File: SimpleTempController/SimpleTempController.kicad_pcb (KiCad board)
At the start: 2 copper layers, 65 x 65 mm, 32 parts, among them J1 Conn_01x01, J2 Conn_01x01, J3 Conn_01x01, J4 Conn_01x01, J5 Conn_01x01, J6 Conn_01x01, Q1 2N2222A, Q4 2N2222A, SW1 SW_Push, SW2 SW_Push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

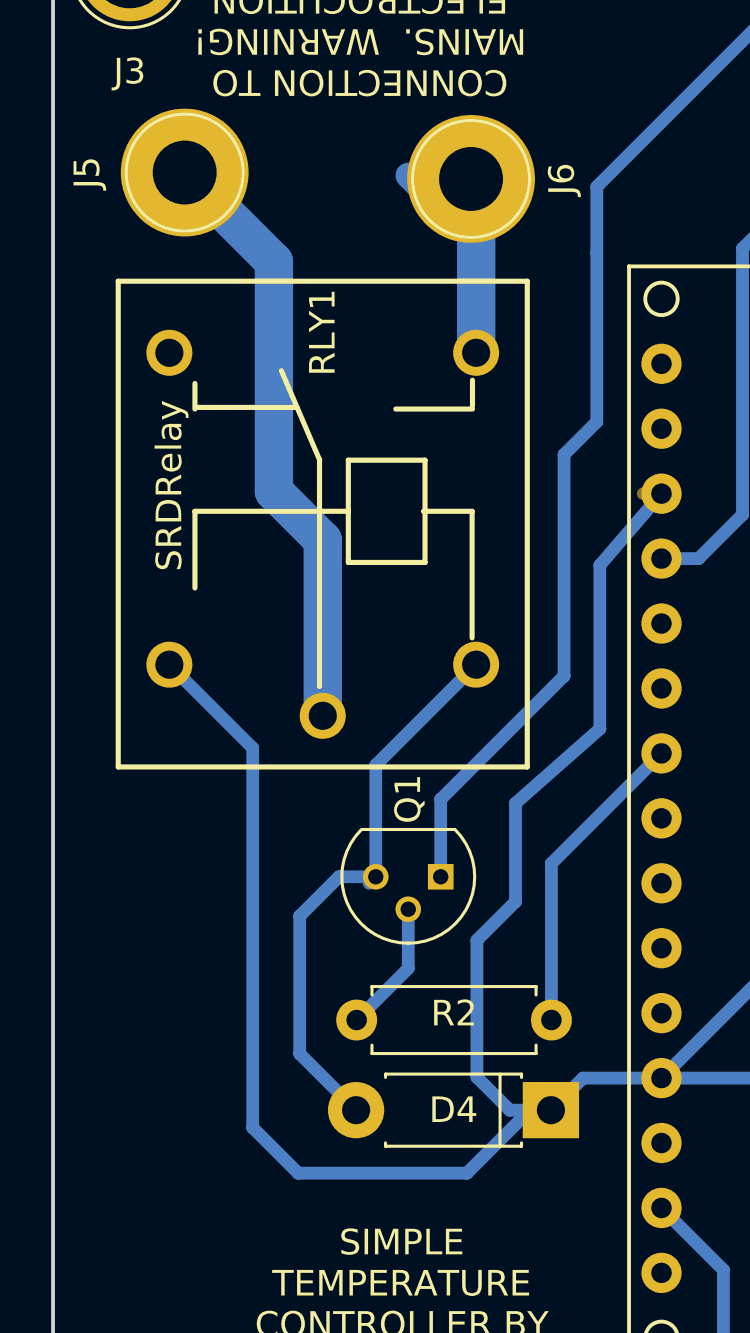
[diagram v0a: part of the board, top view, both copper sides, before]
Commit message: More Creepage
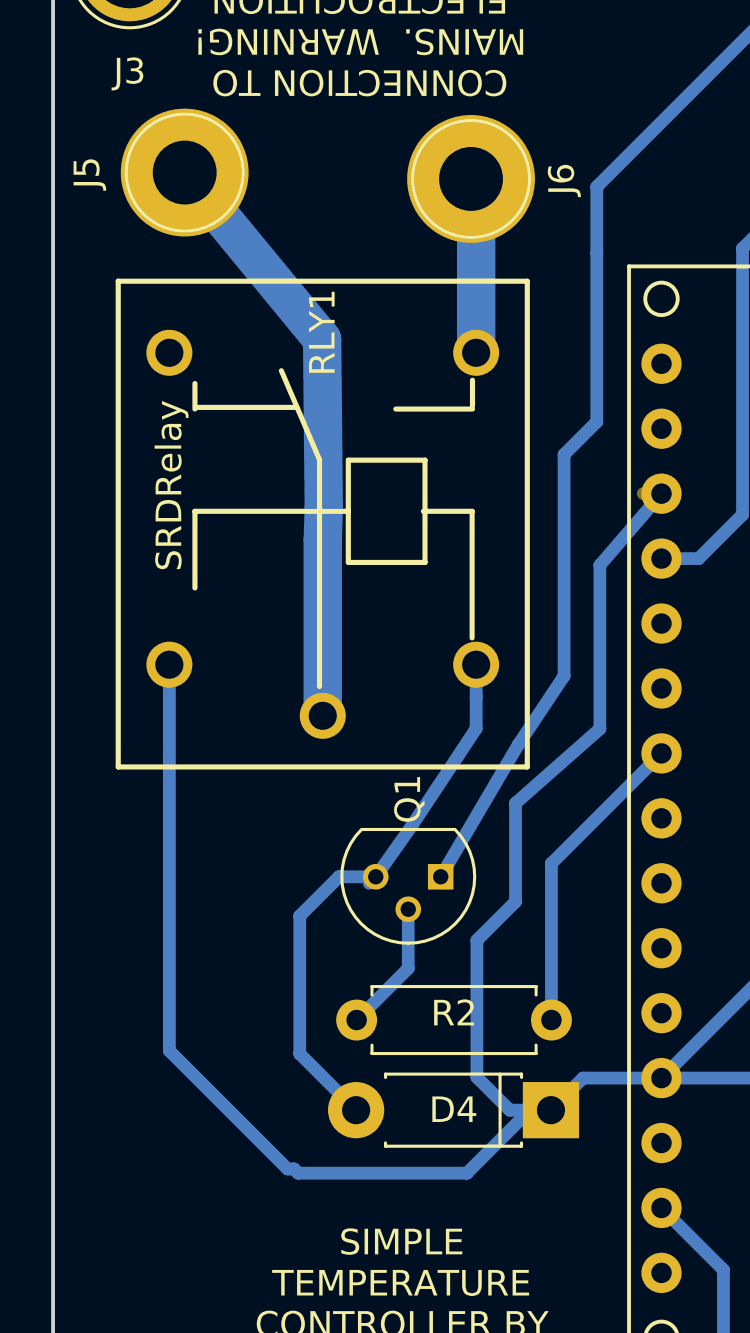
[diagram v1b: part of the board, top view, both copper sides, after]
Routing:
- net GND: track 225.3 -> 224.6 mm
- net Net-(J6-Pad1): track 7.47 -> 6.88 mm
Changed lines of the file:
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@@
     (links 52)
     (no_connects 0)
-    (area 159.924999 39.524999 225.075001 104.675001)
+    (area 158.252381 39.524999 226.74762 105.675)
     (thickness 1.6)
     (drawings 10)
-    (tracks 201)
+    (tracks 203)
     (zones 0)
     (modules 32)
@@
     (effects (font (size 1 1) (thickness 0.15)))
   )
+  (segment (start 169.425 89.525) (end 169.175 89.525) (width 0.5) (layer B.Cu) (net 1))
+  (segment (start 164.55 84.9) (end 164.55 69.8) (width 0.5) (layer B.Cu) (net 1) (status 800000))
+  (segment (start 169.175 89.525) (end 164.55 84.9) (width 0.5) (layer B.Cu) (net 1))
   (segment (start 204.55 51.775) (end 209.55 51.775) (width 0.5) (layer B.Cu) (net 1))
   (segment (start 209.55 51.775) (end 209.9 52.125) (width 0.5) (layer B.Cu) (net 1))
@@
   (segment (start 179.475 87.225) (end 178.655 87.225) (width 0.5) (layer B.Cu) (net 1))
   (segment (start 178.655 87.225) (end 176.19 89.69) (width 0.5) (layer B.Cu) (net 1))
-  (segment (start 167.81 73.06) (end 164.55 69.8) (width 0.5) (layer B.Cu) (net 1))
-  (segment (start 167.81 87.91) (end 167.81 73.06) (width 0.5) (layer B.Cu) (net 1))
-  (segment (start 169.59 89.69) (end 167.81 87.91) (width 0.5) (layer B.Cu) (net 1))
+  (segment (start 169.59 89.69) (end 169.425 89.525) (width 0.5) (layer B.Cu) (net 1))
   (segment (start 176.19 89.69) (end 169.59 89.69) (width 0.5) (layer B.Cu) (net 1))
   (segment (start 179.475 87.225) (end 177.865 87.225) (width 0.5) (layer B.Cu) (net 1))
@@
   (segment (start 222.154 80.128) (end 222.154 96.13) (width 0.5) (layer B.Cu) (net 2))
   (segment (start 204.68 46.725) (end 204.934 46.725) (width 0.5) (layer F.Cu) (net 2) (status 30))
-  (segment (start 175.164 78.096) (end 175.164 75.066) (width 0.5) (layer B.Cu) (net 2))
+  (segment (start 175.164 78.096) (end 178.2 72.925) (width 0.5) (layer B.Cu) (net 2) (status 400000))
   (segment (start 181.27 60.3) (end 181.27 53.7) (width 0.5) (layer B.Cu) (net 2))
   (segment (start 179.99 61.58) (end 181.27 60.3) (width 0.5) (layer B.Cu) (net 2))
   (segment (start 179.99 70.24) (end 179.99 61.58) (width 0.5) (layer B.Cu) (net 2))
-  (segment (start 175.164 75.066) (end 179.99 70.24) (width 0.5) (layer B.Cu) (net 2))
+  (segment (start 178.2 72.925) (end 179.99 70.24) (width 0.5) (layer B.Cu) (net 2))
   (segment (start 219.106 77.334) (end 219.36 77.334) (width 0.5) (layer B.Cu) (net 2))
   (segment (start 202.45 43.64) (end 203.19 43.64) (width 0.5) (layer B.Cu) (net 2))
@@
   (segment (start 217.582 86.224) (end 216.82 86.224) (width 0.5) (layer B.Cu) (net 18))
   (segment (start 216.82 86.224) (end 213.01 90.034) (width 0.5) (layer B.Cu) (net 18))
+  (segment (start 176.55 69.8) (end 176.55 71.05) (width 0.5) (layer B.Cu) (net 19) (status 400000))
+  (segment (start 174.05 76.075) (end 172.624 78.096) (width 0.5) (layer B.Cu) (net 19) (status 800000))
+  (segment (start 176.55 72.3) (end 174.05 76.075) (width 0.5) (layer B.Cu) (net 19))
+  (segment (start 176.55 71.05) (end 176.55 72.3) (width 0.5) (layer B.Cu) (net 19))
   (segment (start 172.624 78.096) (end 171.184 78.096) (width 0.5) (layer B.Cu) (net 19))
   (segment (start 169.65 85.02) (end 171.855 87.225) (width 0.5) (layer B.Cu) (net 19))
   (segment (start 169.65 79.63) (end 169.65 85.02) (width 0.5) (layer B.Cu) (net 19))
   (segment (start 171.184 78.096) (end 169.65 79.63) (width 0.5) (layer B.Cu) (net 19))
-  (segment (start 172.624 78.096) (end 172.624 73.726) (width 0.5) (layer B.Cu) (net 19))
-  (segment (start 172.624 73.726) (end 176.55 69.8) (width 0.5) (layer B.Cu) (net 19))
   (segment (start 172.37 78.35) (end 172.624 78.096) (width 0.5) (layer B.Cu) (net 19))
   (segment (start 205.39 86.732) (end 205.136 86.732) (width 0.5) (layer B.Cu) (net 20))
@@
   (segment (start 213.01 86.224) (end 217.582 81.652) (width 0.5) (layer B.Cu) (net 21))
   (segment (start 170.55 71.8) (end 170.55 64.93) (width 1.5) (layer B.Cu) (net 22))
-  (segment (start 168.64 54.04) (end 165.15 50.55) (width 1.5) (layer B.Cu) (net 22))
-  (segment (start 168.64 63.02) (end 168.64 54.04) (width 1.5) (layer B.Cu) (net 22))
-  (segment (start 170.55 64.93) (end 168.64 63.02) (width 1.5) (layer B.Cu) (net 22))
+  (segment (start 170.525 57.075) (end 165.15 50.55) (width 1.5) (layer B.Cu) (net 22) (status 800000))
+  (segment (start 170.59 63.67) (end 170.525 57.075) (width 1.5) (layer B.Cu) (net 22))
+  (segment (start 170.55 64.93) (end 170.59 63.67) (width 1.5) (layer B.Cu) (net 22))
   (segment (start 176.55 57.6) (end 176.55 51) (width 1.5) (layer B.Cu) (net 23))
   (segment (start 176.55 51) (end 176.35 50.8) (width 1.5) (layer B.Cu) (net 23))
-  (segment (start 174.306 51.076) (end 173.894 50.664) (width 1) (layer B.Cu) (net 23))
   (segment (start 207.676 46.6) (end 207.185 46.6) (width 0.5) (layer B.Cu) (net 24))
   (segment (start 207.185 46.6) (end 204.55 49.235) (width 0.5) (layer B.Cu) (net 24))

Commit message: Even more creepage
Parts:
- moved RLY1 1.74 mm to (169.2, 64.9)
- moved J5 1.56 mm to (164.0, 51.6)
- moved J6 1.36 mm to (175.2, 51.6)
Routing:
- net Net-(D4-Pad2): track 22.0 -> 20.7 mm
- net Net-(J5-Pad1): track 23.2 -> 23.7 mm
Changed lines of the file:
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@@
     (thickness 1.6)
     (drawings 10)
-    (tracks 203)
+    (tracks 200)
     (zones 0)
     (modules 32)
@@
   )
   (setup
-    (last_trace_width 0.5)
+    (last_trace_width 1.5)
     (user_trace_width 0.35)
     (user_trace_width 0.5)
@@
     (mod_text_width 0.15)
     (pad_size 4.064 4.064)
-    (pad_drill 2.2)
+    (pad_drill 3.048)
     (pad_to_mask_clearance 0.2)
     (aux_axis_origin 0 0)
@@
   )
   (module SimpleTempController:SRDXXRelay (layer F.Cu)
-    (at 170.55 63.8 90)
+    (at 169.2 64.9 90)
     (fp_text reference RLY1 (at 7 0 90) (layer F.SilkS)
       (effects (font (size 1 1) (thickness 0.15)))
@@
     (fp_circle (center 0 0) (end 2.6 0) (layer F.CrtYd) (width 0.05))
     (fp_circle (center 0 0) (end 0 -2.286) (layer F.SilkS) (width 0.12))
-    (pad 1 thru_hole circle (at 0 0) (size 4.064 4.064) (drill 3.048) (layers *.Cu *.Mask))
+    (pad "" np_thru_hole circle (at 0 0) (size 4.064 4.064) (drill 3.048) (layers *.Cu *.Mask))
   )
   (module Connectors:1pin (layer F.Cu)
@@
     (fp_circle (center 0 0) (end 2.6 0) (layer F.CrtYd) (width 0.05))
     (fp_circle (center 0 0) (end 0 -2.286) (layer F.SilkS) (width 0.12))
-    (pad 1 thru_hole circle (at 0 0) (size 4.064 4.064) (drill 3.048) (layers *.Cu *.Mask))
+    (pad "" np_thru_hole circle (at 0 0) (size 4.064 4.064) (drill 3.048) (layers *.Cu *.Mask))
   )
   (module Connectors:1pin (layer F.Cu)
@@
     (fp_circle (center 0 0) (end 2.6 0) (layer F.CrtYd) (width 0.05))
     (fp_circle (center 0 0) (end 0 -2.286) (layer F.SilkS) (width 0.12))
-    (pad 1 thru_hole circle (at 0 0) (size 4.064 4.064) (drill 3.048) (layers *.Cu *.Mask))
+    (pad "" np_thru_hole circle (at 0 0) (size 4.064 4.064) (drill 3.048) (layers *.Cu *.Mask))
   )
   (module Connectors:1pin (layer F.Cu)
@@
     (fp_circle (center 0 0) (end 2.6 0) (layer F.CrtYd) (width 0.05))
     (fp_circle (center 0 0) (end 0 -2.286) (layer F.SilkS) (width 0.12))
-    (pad 1 thru_hole circle (at 0 0) (size 4.064 4.064) (drill 3.048) (layers *.Cu *.Mask))
+    (pad "" np_thru_hole circle (at 0 0) (size 4.064 4.064) (drill 3.048) (layers *.Cu *.Mask))
   )
   (module Diodes_THT:D_DO-41_SOD81_P7.62mm_Horizontal (layer F.Cu)
@@
   )
   (module Connectors:1pin (layer F.Cu)
-    (at 165.15 50.55)
+    (at 164 51.6)
     (descr "module 1 pin (ou trou mecanique de percage)")
     (tags DEV)
-    (fp_text reference J5 (at -3.81 0 90) (layer F.SilkS)
+    (fp_text reference J5 (at 3.8 -0.05 90) (layer F.SilkS)
       (effects (font (size 1 1) (thickness 0.15)))
     )
@@
   )
   (module Connectors:1pin (layer F.Cu)
-    (at 176.35 50.8)
+    (at 175.25 51.6)
     (descr "module 1 pin (ou trou mecanique de percage)")
     (tags DEV)
@@
   (gr_line (start 225 39.6) (end 225 104.6) (angle 90) (layer Edge.Cuts) (width 0.15))
   (gr_line (start 160 39.6) (end 225 39.6) (angle 90) (layer Edge.Cuts) (width 0.15))
-  (gr_text "CONNECTION TO\nMAINS.  WARNING!\nELECTROCUTION\nHAZARD!" (at 172 44.6 180) (layer F.SilkS)
+  (gr_text "CONNECTION TO\nMAINS.  WARNING!\nELECTROCUTION\nHAZARD!" (at 173.6 43.9 180) (layer F.SilkS)
     (effects (font (size 1 1) (thickness 0.15)))
   )
@@
     (effects (font (size 1 1) (thickness 0.15)))
   )
-  (segment (start 169.425 89.525) (end 169.175 89.525) (width 0.5) (layer B.Cu) (net 1))
-  (segment (start 164.55 84.9) (end 164.55 69.8) (width 0.5) (layer B.Cu) (net 1) (status 800000))
-  (segment (start 169.175 89.525) (end 164.55 84.9) (width 0.5) (layer B.Cu) (net 1))
+  (segment (start 168.05 89.65) (end 167.8 89.65) (width 0.5) (layer B.Cu) (net 1))
+  (segment (start 163.2 84.325) (end 163.2 70.9) (width 0.5) (layer B.Cu) (net 1) (status 20))
+  (segment (start 167.8 89.65) (end 163.2 84.325) (width 0.5) (layer B.Cu) (net 1))
   (segment (start 204.55 51.775) (end 209.55 51.775) (width 0.5) (layer B.Cu) (net 1))
   (segment (start 209.55 51.775) (end 209.9 52.125) (width 0.5) (layer B.Cu) (net 1))
@@
   (segment (start 179.475 87.225) (end 178.655 87.225) (width 0.5) (layer B.Cu) (net 1))
   (segment (start 178.655 87.225) (end 176.19 89.69) (width 0.5) (layer B.Cu) (net 1))
-  (segment (start 169.59 89.69) (end 169.425 89.525) (width 0.5) (layer B.Cu) (net 1))
+  (segment (start 169.59 89.69) (end 168.05 89.65) (width 0.5) (layer B.Cu) (net 1))
   (segment (start 176.19 89.69) (end 169.59 89.69) (width 0.5) (layer B.Cu) (net 1))
   (segment (start 179.475 87.225) (end 177.865 87.225) (width 0.5) (layer B.Cu) (net 1))
   (segment (start 181.39 65.91) (end 183.8 63.11) (width 0.5) (layer B.Cu) (net 1))
   (segment (start 181.39 72.31) (end 181.39 65.91) (width 0.5) (layer B.Cu) (net 1))
-  (segment (start 178.09 75.22) (end 181.39 72.31) (width 0.5) (layer B.Cu) (net 1))
-  (segment (start 178.09 79.07) (end 178.09 75.22) (width 0.5) (layer B.Cu) (net 1))
+  (segment (start 178.1 77.1) (end 181.39 72.31) (width 0.5) (layer B.Cu) (net 1))
+  (segment (start 178.09 79.07) (end 178.1 77.1) (width 0.5) (layer B.Cu) (net 1))
   (segment (start 176.58 80.58) (end 178.09 79.07) (width 0.5) (layer B.Cu) (net 1))
   (segment (start 176.58 85.94) (end 176.58 80.58) (width 0.5) (layer B.Cu) (net 1))
@@
   (segment (start 214.52 43.64) (end 216.515 45.635) (width 0.5) (layer B.Cu) (net 2))
   (segment (start 216.515 45.635) (end 217.48 46.6) (width 0.5) (layer B.Cu) (net 2))
-  (segment (start 181.27 53.7) (end 181.27 51.105) (width 0.5) (layer B.Cu) (net 2))
+  (segment (start 182.27 52.7) (end 183.2 51.4) (width 0.5) (layer B.Cu) (net 2))
   (segment (start 188.735 43.64) (end 200.16 43.64) (width 0.5) (layer B.Cu) (net 2))
   (segment (start 200.16 43.64) (end 202.45 43.64) (width 0.5) (layer B.Cu) (net 2))
-  (segment (start 181.27 51.105) (end 188.735 43.64) (width 0.5) (layer B.Cu) (net 2))
+  (segment (start 183.2 51.4) (end 188.735 43.64) (width 0.5) (layer B.Cu) (net 2))
   (segment (start 186.2225 96.1525) (end 186.2225 93.4725) (width 0.5) (layer B.Cu) (net 2))
   (segment (start 186.2225 93.4725) (end 183.8 91.05) (width 0.5) (layer B.Cu) (net 2))
@@
   (segment (start 222.154 80.128) (end 222.154 96.13) (width 0.5) (layer B.Cu) (net 2))
   (segment (start 204.68 46.725) (end 204.934 46.725) (width 0.5) (layer F.Cu) (net 2) (status 30))
-  (segment (start 175.164 78.096) (end 178.2 72.925) (width 0.5) (layer B.Cu) (net 2) (status 400000))
-  (segment (start 181.27 60.3) (end 181.27 53.7) (width 0.5) (layer B.Cu) (net 2))
-  (segment (start 179.99 61.58) (end 181.27 60.3) (width 0.5) (layer B.Cu) (net 2))
-  (segment (start 179.99 70.24) (end 179.99 61.58) (width 0.5) (layer B.Cu) (net 2))
-  (segment (start 178.2 72.925) (end 179.99 70.24) (width 0.5) (layer B.Cu) (net 2))
+  (segment (start 175.164 78.096) (end 180.2 72) (width 0.5) (layer B.Cu) (net 2))
+  (segment (start 182.27 59.3) (end 182.27 52.7) (width 0.5) (layer B.Cu) (net 2))
+  (segment (start 180.24 62.08) (end 182.27 59.3) (width 0.5) (layer B.Cu) (net 2))
+  (segment (start 180.24 70.74) (end 180.24 62.08) (width 0.5) (layer B.Cu) (net 2))
+  (segment (start 180.2 72) (end 180.24 70.74) (width 0.5) (layer B.Cu) (net 2))
   (segment (start 219.106 77.334) (end 219.36 77.334) (width 0.5) (layer B.Cu) (net 2))
   (segment (start 202.45 43.64) (end 203.19 43.64) (width 0.5) (layer B.Cu) (net 2))
@@
   (segment (start 217.582 86.224) (end 216.82 86.224) (width 0.5) (layer B.Cu) (net 18))
   (segment (start 216.82 86.224) (end 213.01 90.034) (width 0.5) (layer B.Cu) (net 18))
-  (segment (start 176.55 69.8) (end 176.55 71.05) (width 0.5) (layer B.Cu) (net 19) (status 400000))
-  (segment (start 174.05 76.075) (end 172.624 78.096) (width 0.5) (layer B.Cu) (net 19) (status 800000))
-  (segment (start 176.55 72.3) (end 174.05 76.075) (width 0.5) (layer B.Cu) (net 19))
-  (segment (start 176.55 71.05) (end 176.55 72.3) (width 0.5) (layer B.Cu) (net 19))
+  (segment (start 175.2 75.2) (end 172.624 78.096) (width 0.5) (layer B.Cu) (net 19))
+  (segment (start 175.25 72.2) (end 175.2 75.2) (width 0.5) (layer B.Cu) (net 19))
   (segment (start 172.624 78.096) (end 171.184 78.096) (width 0.5) (layer B.Cu) (net 19))
   (segment (start 169.65 85.02) (end 171.855 87.225) (width 0.5) (layer B.Cu) (net 19))
@@
   (segment (start 171.184 78.096) (end 169.65 79.63) (width 0.5) (layer B.Cu) (net 19))
   (segment (start 172.37 78.35) (end 172.624 78.096) (width 0.5) (layer B.Cu) (net 19))
+  (segment (start 175.2 70.9) (end 175.25 70.95) (width 0.5) (layer B.Cu) (net 19) (status 10))
+  (segment (start 175.25 70.95) (end 175.25 72.2) (width 0.5) (layer B.Cu) (net 19))
   (segment (start 205.39 86.732) (end 205.136 86.732) (width 0.5) (layer B.Cu) (net 20))
   (segment (start 205.136 86.732) (end 204.12 85.716) (width 0.5) (layer B.Cu) (net 20))
@@
   (segment (start 213.01 86.732) (end 213.01 86.224) (width 0.5) (layer B.Cu) (net 21))
   (segment (start 213.01 86.224) (end 217.582 81.652) (width 0.5) (layer B.Cu) (net 21))
-  (segment (start 170.55 71.8) (end 170.55 64.93) (width 1.5) (layer B.Cu) (net 22))
-  (segment (start 170.525 57.075) (end 165.15 50.55) (width 1.5) (layer B.Cu) (net 22) (status 800000))
-  (segment (start 170.59 63.67) (end 170.525 57.075) (width 1.5) (layer B.Cu) (net 22))
-  (segment (start 170.55 64.93) (end 170.59 63.67) (width 1.5) (layer B.Cu) (net 22))
-  (segment (start 176.55 57.6) (end 176.55 51) (width 1.5) (layer B.Cu) (net 23))
-  (segment (start 176.55 51) (end 176.35 50.8) (width 1.5) (layer B.Cu) (net 23))
+  (segment (start 169.2 72.9) (end 169.25 56.1) (width 1.5) (layer B.Cu) (net 22) (status 10))
+  (segment (start 169.25 56.1) (end 164 51.6) (width 1.5) (layer B.Cu) (net 22) (status 20))
+  (segment (start 175.2 58.7) (end 175.25 51.6) (width 1.5) (layer B.Cu) (net 23) (status 20))
   (segment (start 207.676 46.6) (end 207.185 46.6) (width 0.5) (layer B.Cu) (net 24))
   (segment (start 207.185 46.6) (end 204.55 49.235) (width 0.5) (layer B.Cu) (net 24))
